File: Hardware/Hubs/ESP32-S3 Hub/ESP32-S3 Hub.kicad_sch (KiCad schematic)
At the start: 27 parts, among them U1 ESP32-S3, Y1 ABM11-40.000MHZ-B1U-T3, 10ppm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

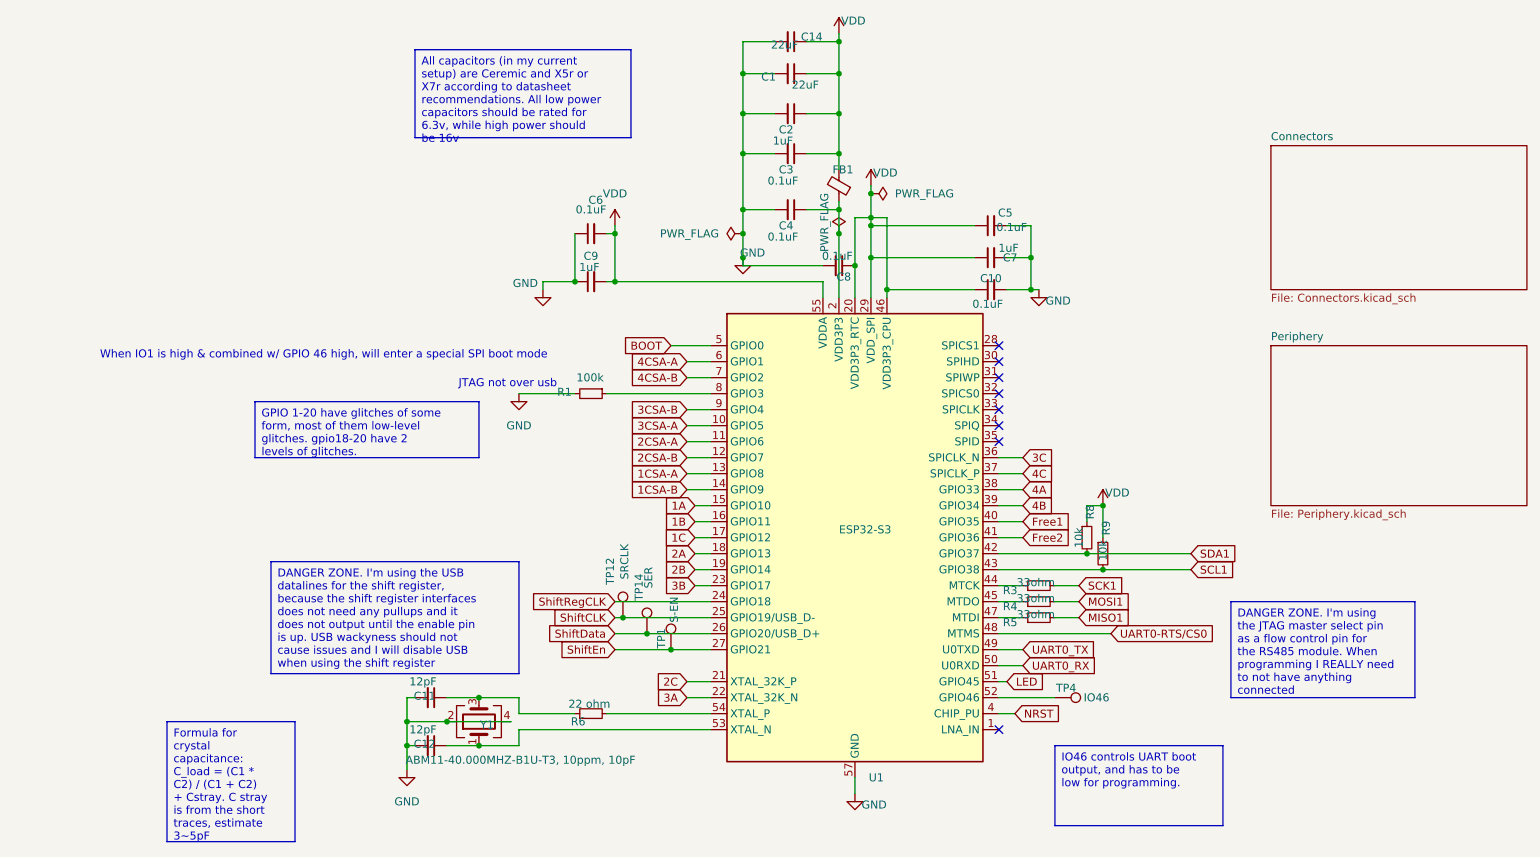
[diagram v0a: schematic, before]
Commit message: Updated connectors in schem and pcb
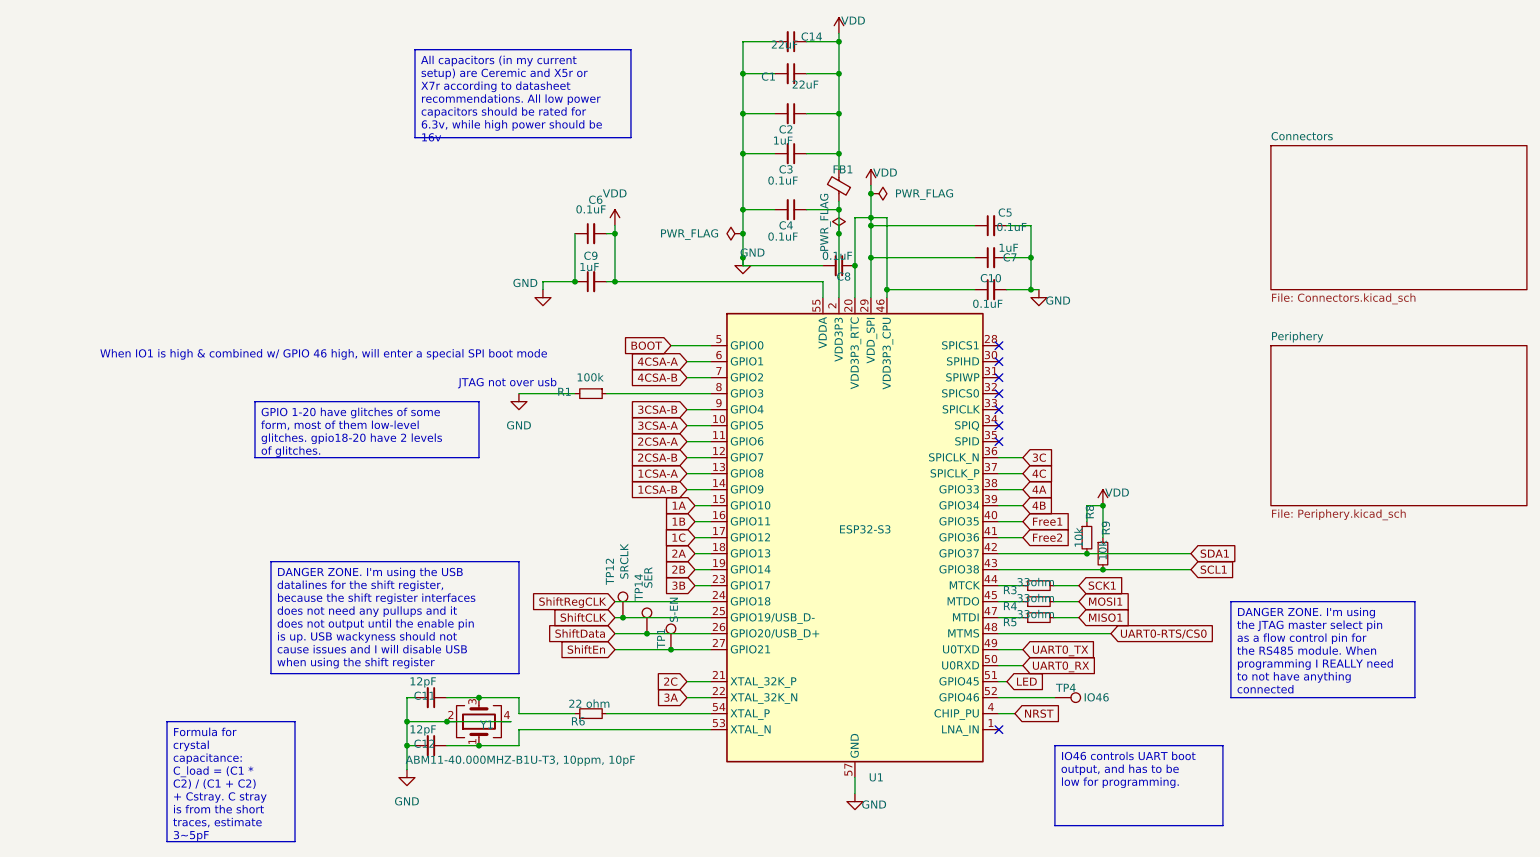
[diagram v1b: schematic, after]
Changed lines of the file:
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@@
 (kicad_sch
-	(version 20231120)
+	(version 20250114)
 	(generator "eeschema")
-	(generator_version "8.0")
+	(generator_version "9.0")
 	(paper "A4")
 	(title_block
 		(title "CACKLE -  Hub")
-		(date "2024-10-08")
-		(rev "V1")
+		(date "2025-10-10")
+		(rev "V1.1")
 		(comment 1 "Licensed under CERN-OHL-S v2")
 		(comment 2 "Author: Asher Edwards")
 	)
+	(text "JTAG not over usb"
+		(exclude_from_sim no)
+		(at 89.662 68.326 0)
+		(effects
+			(font
+				(size 1.27 1.27)
+			)
+		)
+	)
+	(text "When IO1 is high & combined w/ GPIO 46 high, will enter a special SPI boot mode"
+		(exclude_from_sim no)
+		(at 60.452 63.754 0)
+		(effects
+			(font
+				(size 1.27 1.27)
+			)
+		)
+	)
+	(text_box "DANGER ZONE. I'm using the JTAG master select pin as a flow control pin for the RS485 module. When programming I REALLY need to not have anything connected"
+		(exclude_from_sim no)
+		(at 204.47 102.87 0)
+		(size 29.21 15.24)
+		(margins 0.9525 0.9525 0.9525 0.9525)
+		(stroke
+			(width 0)
+			(type default)
+		)
+		(fill
+			(type none)
+		)
+		(effects
+			(font
+				(size 1.27 1.27)
+			)
+			(justify left top)
+		)
+	)
+	(text_box "DANGER ZONE. I'm using the USB datalines for the shift register, because the shift register interfaces does not need any pullups and it does not output until the enable pin is up. USB wackyness should not cause issues and I will disable USB when using the shift register"
+		(exclude_from_sim no)
+		(at 52.07 96.52 0)
+		(size 39.37 17.78)
+		(margins 0.9525 0.9525 0.9525 0.9525)
+		(stroke
+			(width 0)
+			(type default)
+		)
+		(fill
+			(type none)
+		)
+		(effects
+			(font
+				(size 1.27 1.27)
+			)
+			(justify left top)
+		)
+	)
+	(text_box "All capacitors (in my current setup) are Ceremic and X5r or X7r according to datasheet recommendations. All low power capacitors should be rated for 6.3v, while high power should be 16v"
+		(exclude_from_sim no)
+		(at 74.93 15.24 0)
+		(size 34.29 13.97)
+		(margins 0.9525 0.9525 0.9525 0.9525)
+		(stroke
+			(width 0)
+			(type default)
+		)
+		(fill
+			(type none)
+		)
+		(effects
+			(font
+				(size 1.27 1.27)
+			)
+			(justify left top)
+		)
+	)
+	(text_box "IO46 controls UART boot output, and has to be low for programming."
+		(exclude_from_sim no)
+		(at 176.53 125.73 0)
+		(size 26.67 12.7)
+		(margins 0.9525 0.9525 0.9525 0.9525)
+		(stroke
+			(width 0)
+			(type default)
+		)
+		(fill
+			(type none)
+		)
+		(effects
+			(font
+				(size 1.27 1.27)
+			)
+			(justify left top)
+		)
+	)
+	(text_box "GPIO 1-20 have glitches of some form, most of them low-level glitches. gpio18-20 have 2 levels of glitches. "
+		(exclude_from_sim no)
+		(at 49.53 71.12 0)
+		(size 35.56 8.89)
+		(margins 0.9525 0.9525 0.9525 0.9525)
+		(stroke
+			(width 0)
+			(type default)
+		)
+		(fill
+			(type none)
+		)
+		(effects
+			(font
+				(size 1.27 1.27)
+			)
+			(justify left top)
+		)
+	)
+	(text_box "Formula for crystal capacitance: C_load = (C1 * C2) / (C1 + C2) + Cstray. C stray is from the short traces, estimate 3~5pF"
+		(exclude_from_sim no)
+		(at 35.56 121.92 0)
+		(size 20.32 19.05)
+		(margins 0.9525 0.9525 0.9525 0.9525)
+		(stroke
+			(width 0)
+			(type default)
+		)
+		(fill
+			(type none)
+		)
+		(effects
+			(font
+				(size 1.27 1.27)
+			)
+			(justify left top)
+		)
+	)
 	(junction
 		(at 85.09 125.73)
@@
 		)
 	)
-	(text_box "DANGER ZONE. I'm using the JTAG master select pin as a flow control pin for the RS485 module. When programming I REALLY need to not have anything connected"
-		(exclude_from_sim no)
-		(at 204.47 102.87 0)
-		(size 29.21 15.24)
-		(stroke
-			(width 0)
-			(type default)
-		)
-		(fill
-			(type none)
-		)
-		(effects
-			(font
-				(size 1.27 1.27)
-			)
-			(justify left top)
-		)
-	)
-	(text_box "DANGER ZONE. I'm using the USB datalines for the shift register, because the shift register interfaces does not need any pullups and it does not output until the enable pin is up. USB wackyness should not cause issues and I will disable USB when using the shift register"
-		(exclude_from_sim no)
-		(at 52.07 96.52 0)
-		(size 39.37 17.78)
-		(stroke
-			(width 0)
-			(type default)
-		)
-		(fill
-			(type none)
-		)
-		(effects
-			(font
-				(size 1.27 1.27)
-			)
-			(justify left top)
-		)
-	)
-	(text_box "All capacitors (in my current setup) are Ceremic and X5r or X7r according to datasheet recommendations. All low power capacitors should be rated for 6.3v, while high power should be 16v"
-		(exclude_from_sim no)
-		(at 74.93 15.24 0)
-		(size 34.29 13.97)
-		(stroke
-			(width 0)
-			(type default)
-		)
-		(fill
-			(type none)
-		)
-		(effects
-			(font
-				(size 1.27 1.27)
-			)
-			(justify left top)
-		)
-	)
-	(text_box "IO46 controls UART boot output, and has to be low for programming."
-		(exclude_from_sim no)
-		(at 176.53 125.73 0)
-		(size 26.67 12.7)
-		(stroke
-			(width 0)
-			(type default)
-		)
-		(fill
-			(type none)
-		)
-		(effects
-			(font
-				(size 1.27 1.27)
-			)
-			(justify left top)
-		)
-	)
-	(text_box "GPIO 1-20 have glitches of some form, most of them low-level glitches. gpio18-20 have 2 levels of glitches. "
-		(exclude_from_sim no)
-		(at 49.53 71.12 0)
-		(size 35.56 8.89)
-		(stroke
-			(width 0)
-			(type default)
-		)
-		(fill
-			(type none)
-		)
-		(effects
-			(font
-				(size 1.27 1.27)
-			)
-			(justify left top)
-		)
-	)
-	(text_box "Formula for crystal capacitance: C_load = (C1 * C2) / (C1 + C2) + Cstray. C stray is from the short traces, estimate 3~5pF"
-		(exclude_from_sim no)
-		(at 35.56 121.92 0)
-		(size 20.32 19.05)
-		(stroke
-			(width 0)
-			(type default)
-		)
-		(fill
-			(type none)
-		)
-		(effects
-			(font
-				(size 1.27 1.27)
-			)
-			(justify left top)
-		)
-	)
-	(text "JTAG not over usb"
-		(exclude_from_sim no)
-		(at 89.662 68.326 0)
-		(effects
-			(font
-				(size 1.27 1.27)
-			)
-		)
-	)
-	(text "When IO1 is high & combined w/ GPIO 46 high, will enter a special SPI boot mode"
-		(exclude_from_sim no)
-		(at 60.452 63.754 0)
-		(effects
-			(font
-				(size 1.27 1.27)
-			)
-		)
-	)
 	(global_label "2CSA-A"
 		(shape input)
@@
 		(at 210.82 62.23)
 		(size 40.64 25.4)
+		(exclude_from_sim no)
+		(in_bom yes)
+		(on_board yes)
+		(dnp no)
 		(fields_autoplaced yes)
 		(stroke
@@
 		(at 210.82 30.48)
 		(size 40.64 22.86)
+		(exclude_from_sim no)
+		(in_bom yes)
+		(on_board yes)
+		(dnp no)
 		(fields_autoplaced yes)
 		(stroke
@@
 		)
 	)
+	(embedded_fonts no)
 )

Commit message: Changed peripheral, tied PWM to shift reg, program pins
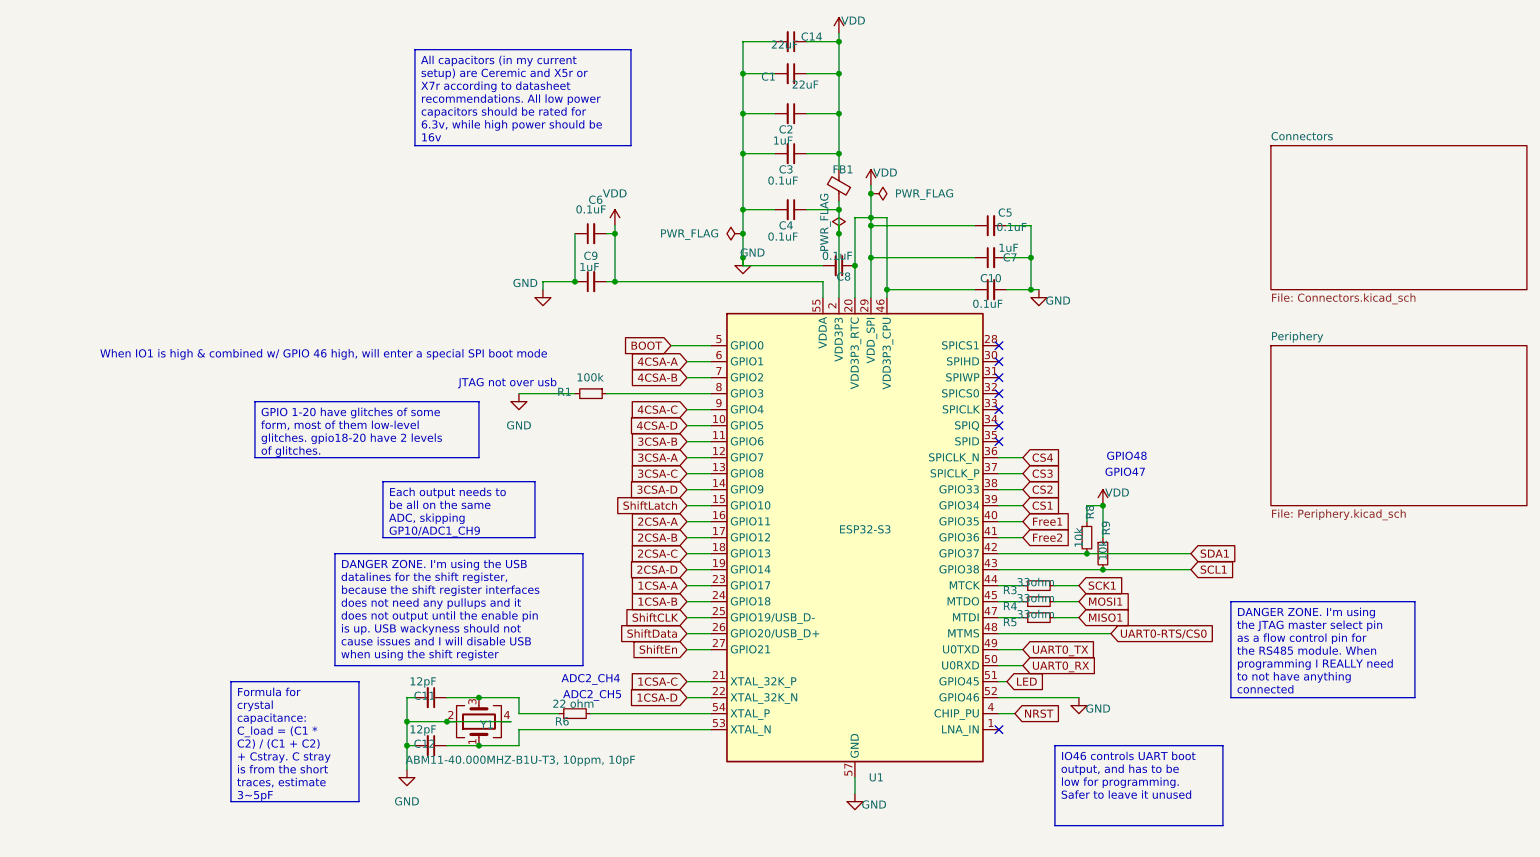
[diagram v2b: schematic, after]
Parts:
- removed TP1: S-EN, TestPoint:TestPoint_Pad_D1.0mm, symbol Connector:TestPoint
- removed TP12: SRCLK, TestPoint:TestPoint_Pad_D1.0mm, symbol Connector:TestPoint
- removed TP14: SER, TestPoint:TestPoint_Pad_D1.0mm, symbol Connector:TestPoint
- removed TP4: IO46, TestPoint:TestPoint_Pad_D1.0mm, symbol Connector:TestPoint
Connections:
- net 1B is gone; now on net 2CSA-A: U1.16 (GPIO11)
- net 1C is gone; now on net 2CSA-B: U1.17 (GPIO12)
- net 3B is gone; now on net 1CSA-A: U1.23 (GPIO17)
- net ShiftRegCLK is gone; now on net 1CSA-B: U1.24 (GPIO18)
- net 1CSA-A: no longer U1.13 (GPIO8)
- net 1CSA-B: no longer U1.14 (GPIO9)
- net 2CSA-A: no longer U1.11 (GPIO6)
- net 2CSA-B: no longer U1.12 (GPIO7)
- net 3CSA-A: now also U1.12 (GPIO7); no longer U1.10 (GPIO5)
- net 3CSA-B: now also U1.11 (GPIO6); no longer U1.9 (GPIO4)
- net GND: now also U1.52 (GPIO46)
- net 1A renamed ShiftLatch
- net 2A renamed 2CSA-C
- net 2B renamed 2CSA-D
- net 2C renamed 1CSA-C
- net 3A renamed 1CSA-D
- net 3C renamed CS4
- net 4A renamed CS2
- net 4B renamed CS1
- net 4C renamed CS3
- new net 3CSA-C: U1.13 (GPIO8)
- new net 3CSA-D: U1.14 (GPIO9)
- new net 4CSA-C: U1.9 (GPIO4)
- new net 4CSA-D: U1.10 (GPIO5)
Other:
- note added: "ADC2_CH4"
- note added: "ADC2_CH5"
- note added: "GPIO47"
- note added: "GPIO48"
- moved on the sheet: R6

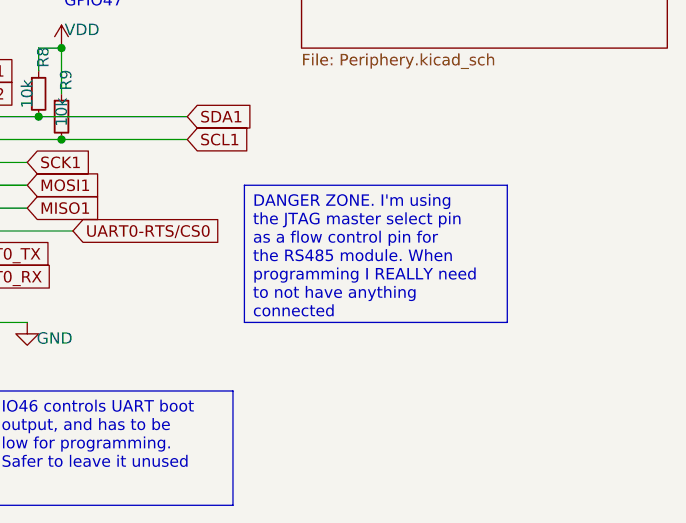
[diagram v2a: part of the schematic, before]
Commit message: Added future design expansion comments, re arrange components to fit better
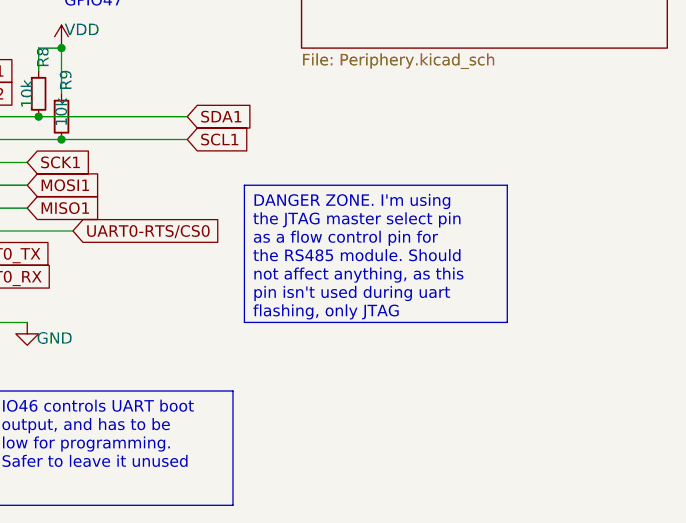
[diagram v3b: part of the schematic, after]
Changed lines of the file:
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@@
 		)
 	)
-	(text_box "DANGER ZONE. I'm using the JTAG master select pin as a flow control pin for the RS485 module. When programming I REALLY need to not have anything connected"
+	(text_box "DANGER ZONE. I'm using the JTAG master select pin as a flow control pin for the RS485 module. Should not affect anything, as this pin isn't used during uart flashing, only JTAG"
 		(exclude_from_sim no)
 		(at 204.47 102.87 0)
@@
 		(stroke
 			(width 0)
-			(type default)
+			(type solid)
 		)
 		(fill

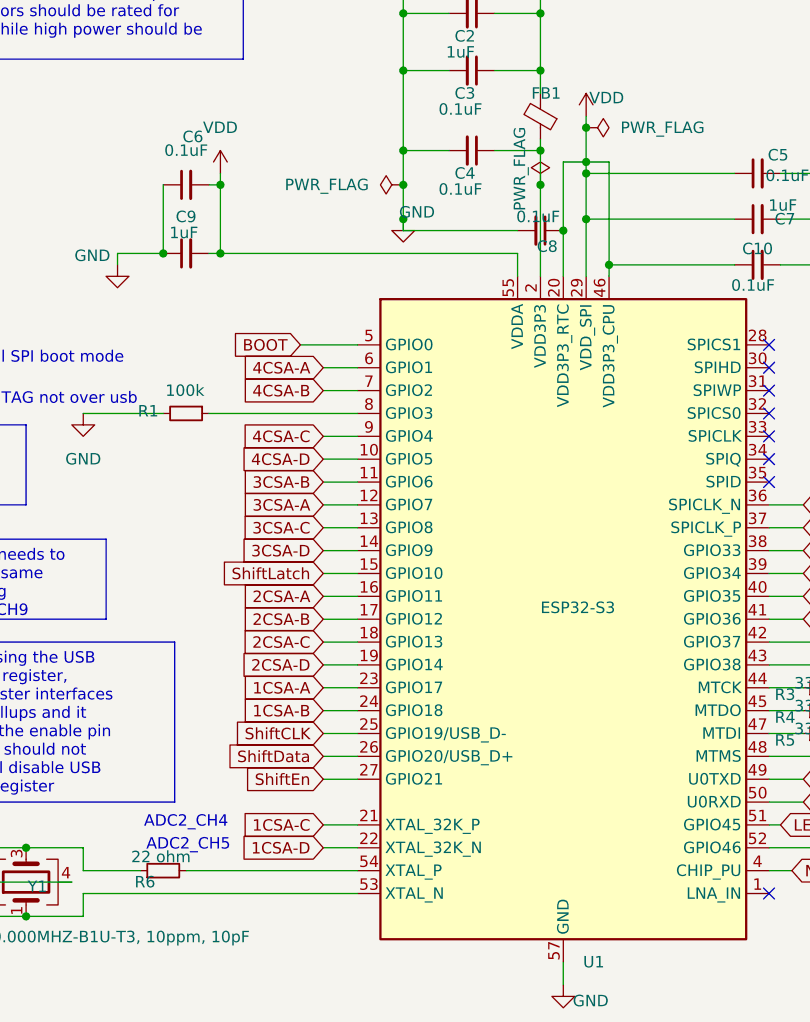
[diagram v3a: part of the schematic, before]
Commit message: Swapped around pins and routed main driver outputs
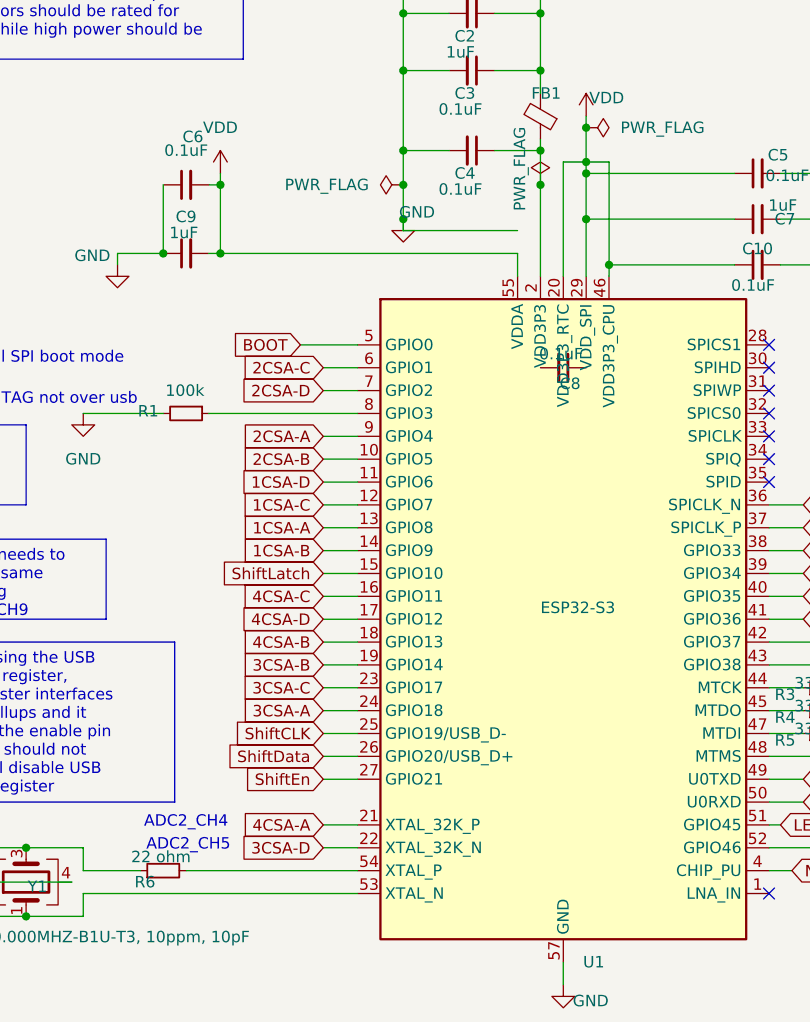
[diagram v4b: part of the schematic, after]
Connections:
- net 1CSA-A: now also U1.13 (GPIO8); no longer U1.23 (GPIO17)
- net 1CSA-B: now also U1.14 (GPIO9); no longer U1.24 (GPIO18)
- net 1CSA-C: now also U1.12 (GPIO7); no longer U1.21 (XTAL_32K_P)
- net 1CSA-D: now also U1.11 (GPIO6); no longer U1.22 (XTAL_32K_N)
- net 2CSA-A: now also U1.9 (GPIO4); no longer U1.16 (GPIO11)
- net 2CSA-B: now also U1.10 (GPIO5); no longer U1.17 (GPIO12)
- net 2CSA-C: now also U1.6 (GPIO1); no longer U1.18 (GPIO13)
- net 2CSA-D: now also U1.7 (GPIO2); no longer U1.19 (GPIO14)
- net 3CSA-A: now also U1.24 (GPIO18); no longer U1.12 (GPIO7)
- net 3CSA-B: now also U1.19 (GPIO14); no longer U1.11 (GPIO6)
- net 3CSA-C: now also U1.23 (GPIO17); no longer U1.13 (GPIO8)
- net 3CSA-D: now also U1.22 (XTAL_32K_N); no longer U1.14 (GPIO9)
- net 4CSA-A: now also U1.21 (XTAL_32K_P); no longer U1.6 (GPIO1)
- net 4CSA-B: now also U1.18 (GPIO13); no longer U1.7 (GPIO2)
- net 4CSA-C: now also U1.16 (GPIO11); no longer U1.9 (GPIO4)
- net 4CSA-D: now also U1.17 (GPIO12); no longer U1.10 (GPIO5)
- net GND: no longer C8.2
- net VDD: no longer C8.1
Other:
- moved on the sheet: C8
